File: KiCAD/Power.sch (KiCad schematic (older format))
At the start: 6 parts, among them J1 170V, J2 5V, J3 3.3V

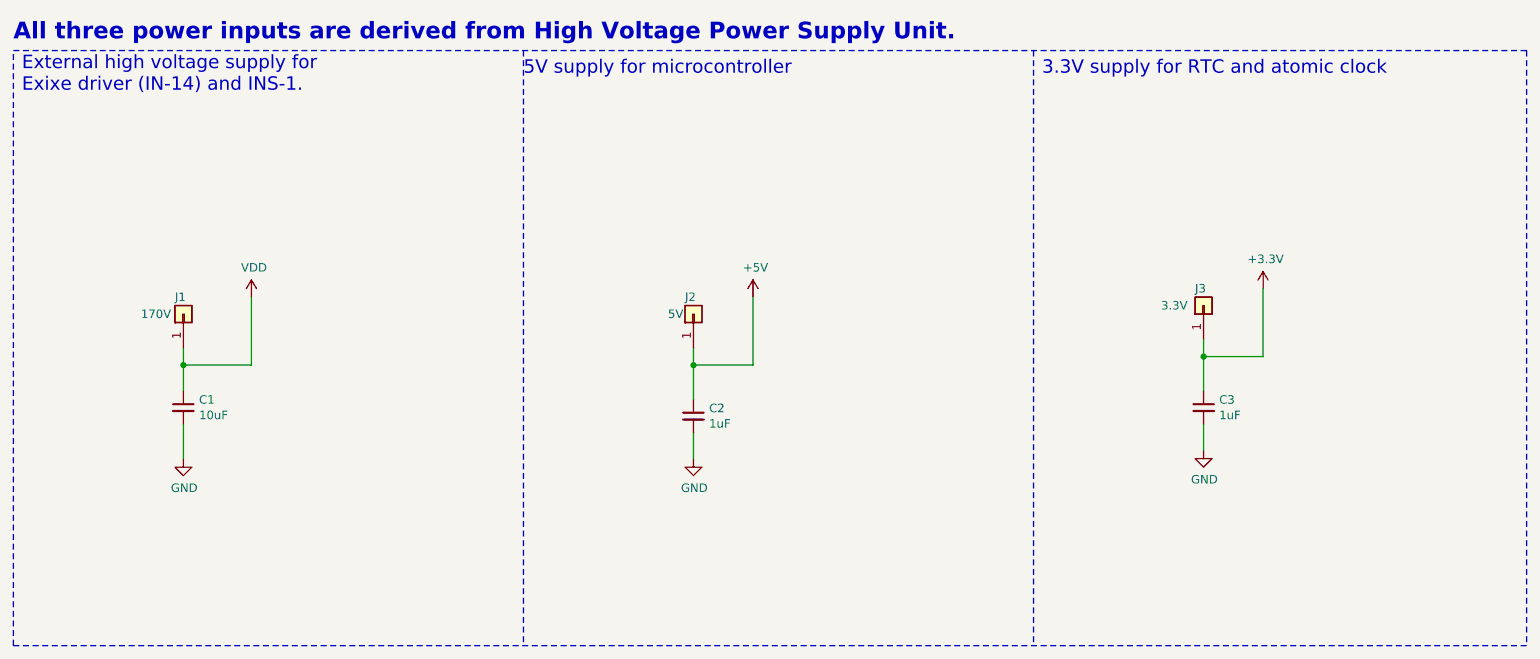
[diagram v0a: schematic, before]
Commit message: v01.2: Updated component numbers, title block, and added transistor library.
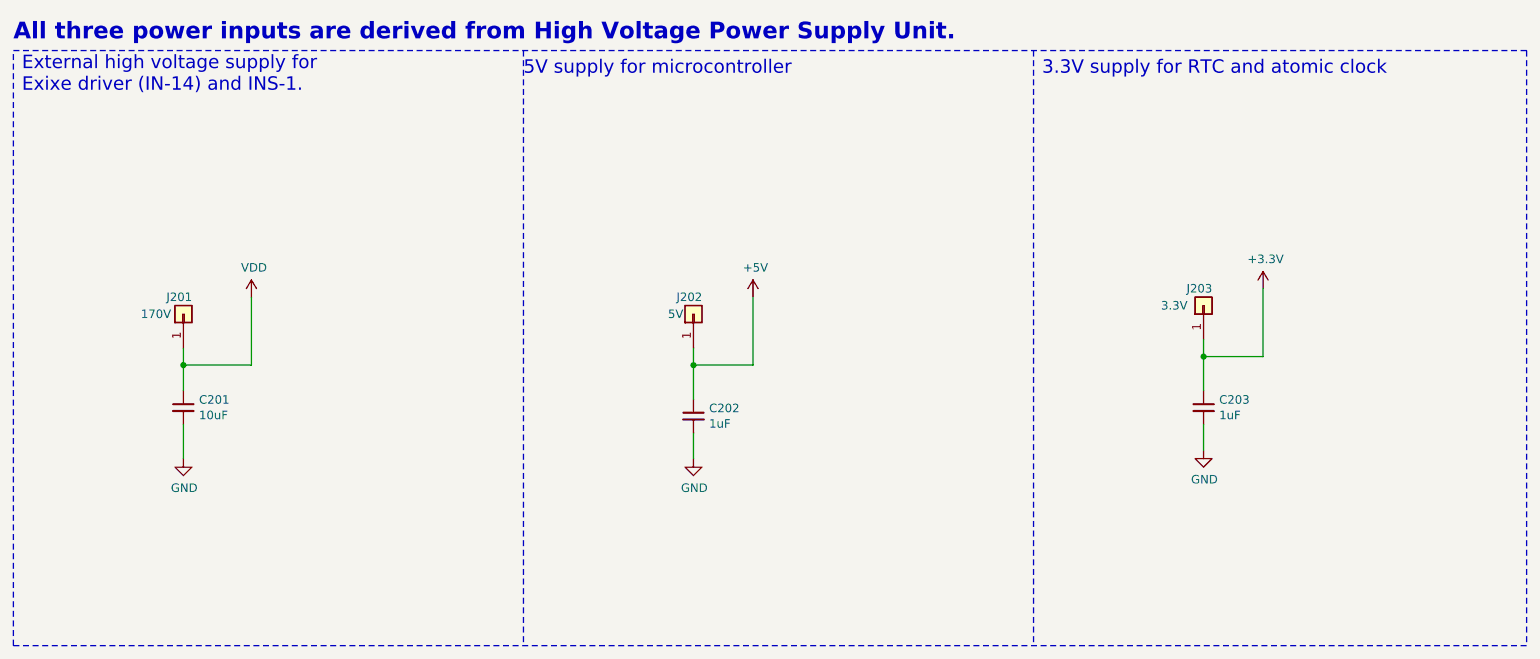
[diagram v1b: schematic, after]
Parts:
- renumbered C1 to C201, C2 to C202, C3 to C203, J1 to J201, J2 to J202, J3 to J203
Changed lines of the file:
@@
 Sheet 2 5
 Title "Nixie Tube Clock Host Board"
-Date "2021-04-20"
-Rev "v01.1"
+Date "2021-04-26"
+Rev "v01.2"
 Comp "University of Alberta (AlbertaSat)"
-Comment1 "License: CC BY 4.0 (https://creativecommons.org/licenses/by/4.0/)"
-Comment2 "Steven Knudsen (ECE dept., Faculty of Engineering, University of Alberta)."
-Comment3 "This schematic was designed with the assistance of "
-Comment4 "Author: Pundeep Hundal                   Co-author: Sichun Xu"
+Comment1 ""
+Comment2 "License: CC BY 4.0 (https://creativecommons.org/licenses/by/4.0/)"
+Comment3 "Co-author: Sichun Xu"
+Comment4 "Author: Pundeep Hundal"
 $EndDescr
 $Comp
-L Connector_Generic:Conn_01x01 J1
+L Connector_Generic:Conn_01x01 J201
 U 1 1 60925BA8
 P 2500 3050
-F 0 "J1" V 2600 3100 50  0000 R CNN
+F 0 "J201" V 2600 3150 50  0000 R CNN
 F 1 "170V" V 2500 3300 50  0000 R CNN
 F 2 "" H 2500 3050 50  0001 C CNN
@@
 $EndComp
 $Comp
-L Connector_Generic:Conn_01x01 J2
+L Connector_Generic:Conn_01x01 J202
 U 1 1 60926684
 P 5500 3050
-F 0 "J2" V 5600 3100 50  0000 R CNN
+F 0 "J202" V 5600 3150 50  0000 R CNN
 F 1 "5V" V 5500 3200 50  0000 R CNN
 F 2 "" H 5500 3050 50  0001 C CNN
@@
 $EndComp
 $Comp
-L Device:C_Small C1
+L Device:C_Small C201
 U 1 1 6092E1DA
 P 2500 3600
-F 0 "C1" H 2592 3646 50  0000 L CNN
+F 0 "C201" H 2592 3646 50  0000 L CNN
 F 1 "10uF" H 2592 3555 50  0000 L CNN
 F 2 "" H 2500 3600 50  0001 C CNN
@@
 $EndComp
 $Comp
-L Device:C_Small C2
+L Device:C_Small C202
 U 1 1 60939809
 P 5500 3650
-F 0 "C2" H 5592 3696 50  0000 L CNN
+F 0 "C202" H 5592 3696 50  0000 L CNN
 F 1 "1uF" H 5592 3605 50  0000 L CNN
 F 2 "" H 5500 3650 50  0001 C CNN
@@
 	8500 3200 8500 3300
 $Comp
-L Device:C_Small C3
+L Device:C_Small C203
 U 1 1 6093035A
 P 8500 3600
-F 0 "C3" H 8592 3646 50  0000 L CNN
+F 0 "C203" H 8592 3646 50  0000 L CNN
 F 1 "1uF" H 8592 3555 50  0000 L CNN
 F 2 "" H 8500 3600 50  0001 C CNN
@@
 $EndComp
 $Comp
-L Connector_Generic:Conn_01x01 J3
+L Connector_Generic:Conn_01x01 J203
 U 1 1 60926D85
 P 8500 3000
-F 0 "J3" V 8600 3050 50  0000 R CNN
+F 0 "J203" V 8600 3100 50  0000 R CNN
 F 1 "3.3V" V 8500 3250 50  0000 R CNN
 F 2 "" H 8500 3000 50  0001 C CNN
